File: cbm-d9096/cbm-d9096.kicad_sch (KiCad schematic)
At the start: 31 parts, among them J1 IEEE488 Header, J2 LED, J3 SD CARD, J4 WP/CD Jumper, J5 SD CARD, J6 WP/CD Jumper, J7 RESET, J8 Alt PWR, J9 Barrel_Jack, U1 ATmega1284-P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

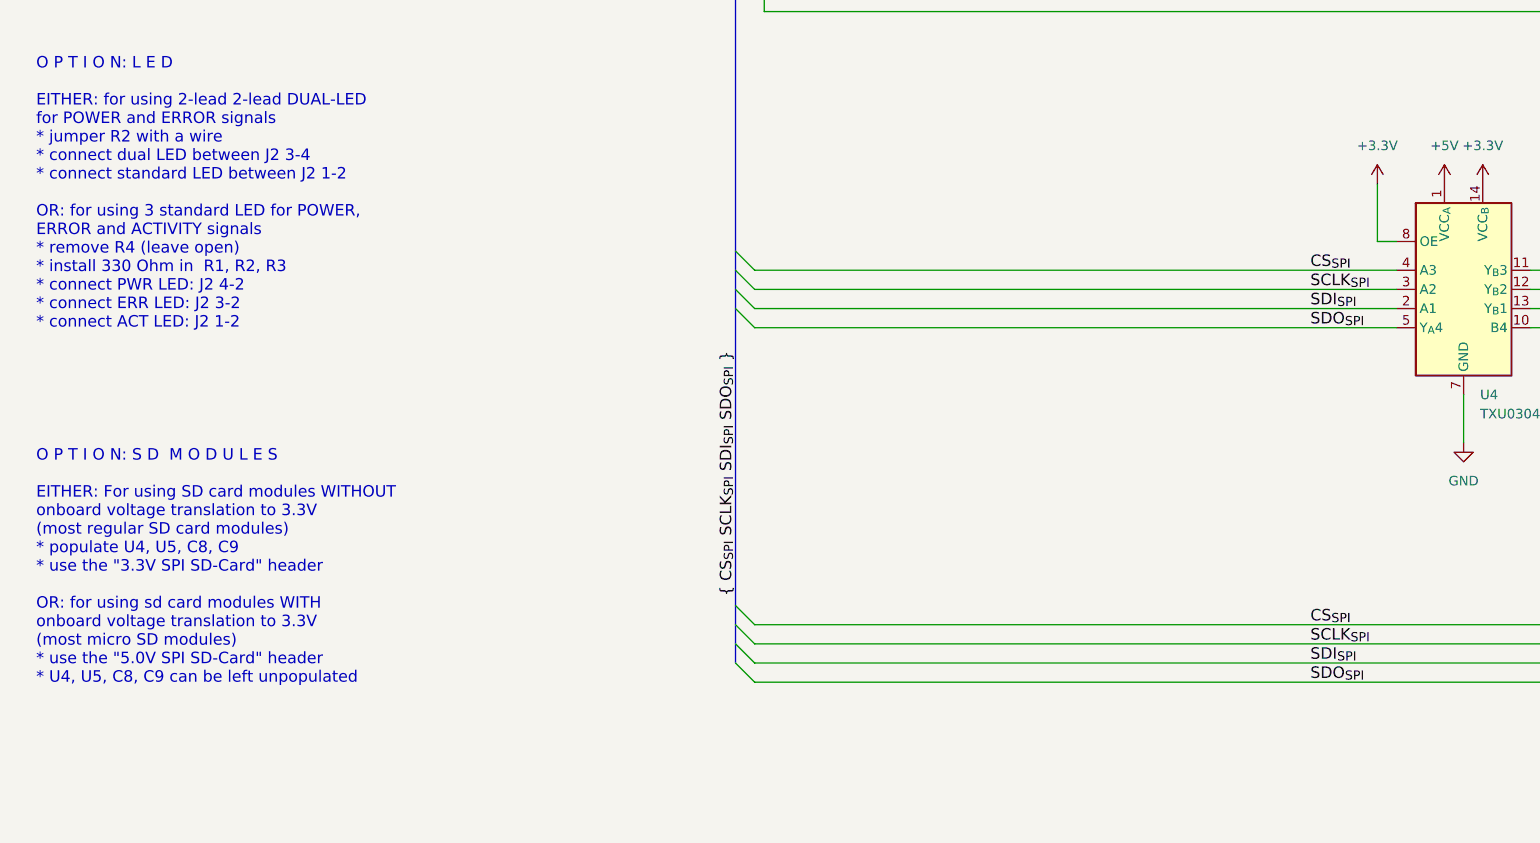
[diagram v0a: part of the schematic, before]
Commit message: added jumper to quickly enable/disable the level shifter
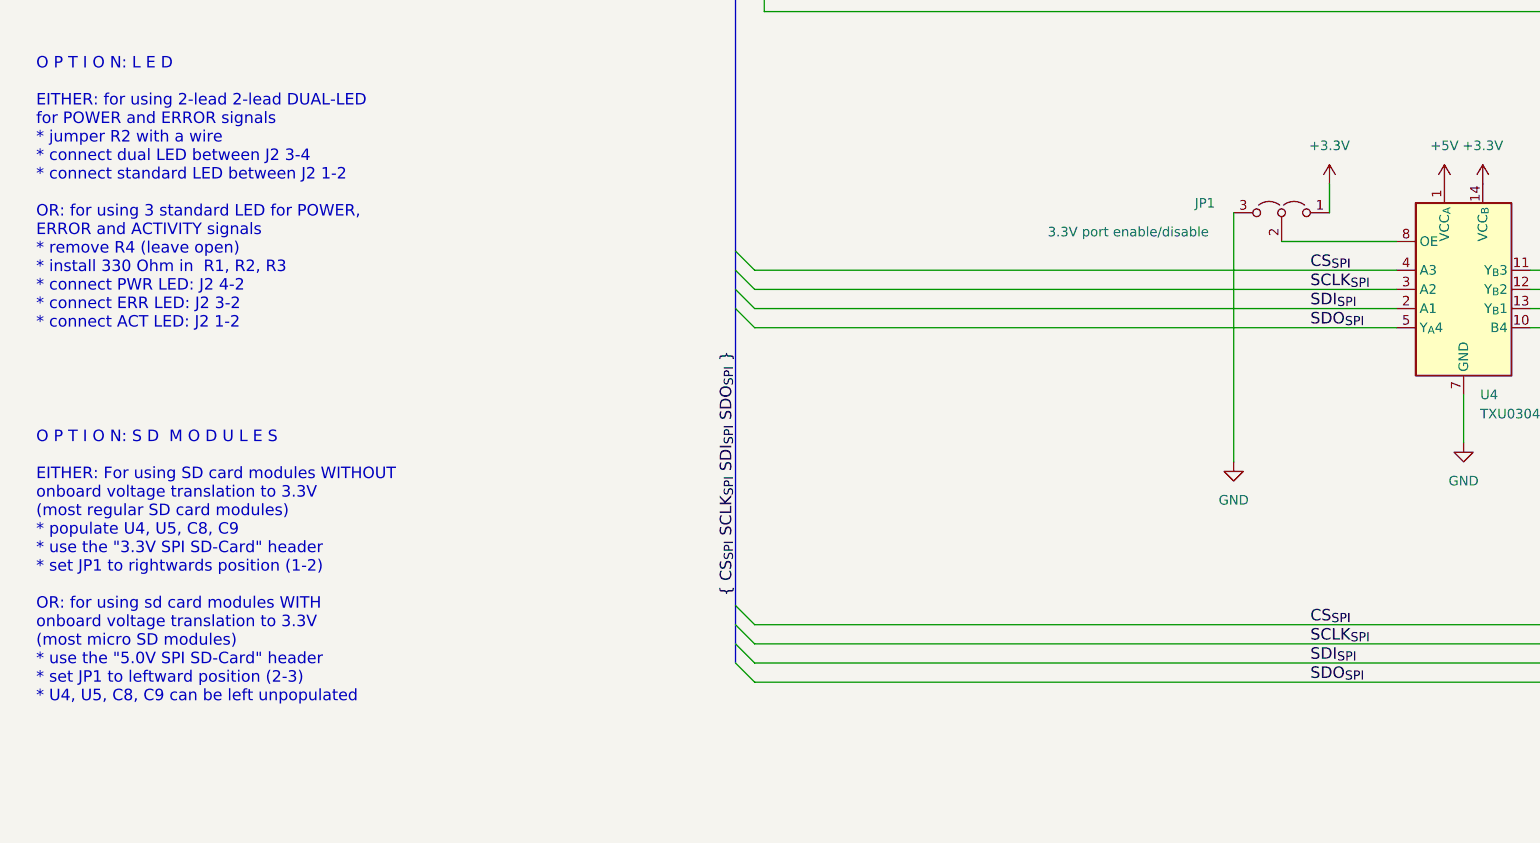
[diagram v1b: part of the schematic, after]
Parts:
- added JP1: 3.3V port enable/disable, Connector_PinHeader_2.00mm:PinHeader_1x03_P2.00mm_Vertical, symbol Jumper:Jumper_3_Open
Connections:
- net +3.3V: now also JP1.1 (A); no longer U4.8 (OE)
- net GND: now also JP1.3 (B)
- new net: JP1.2 (C), U4.8 (OE)
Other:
- note added: "O P T I O N: S D M O D U L E S EITHER: For using SD card modules WITHOUT onboard voltage translation to 3.3V (most regular SD card modules) * populate U4, U5, C8, C9 * use the "3.3V SPI SD-Card" header * set JP1 to rightwards position (1-2) OR: for using sd card modules WITH onboard voltage translation to 3.3V (most micro SD modules) * use the "5.0V SPI SD-Card" header * set JP1 to leftward posit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"
- note removed: "O P T I O N: S D M O D U L E S EITHER: For using SD card modules WITHOUT onboard voltage translation to 3.3V (most regular SD card modules) * populate U4, U5, C8, C9 * use the "3.3V SPI SD-Card" header OR: for using sd card modules WITH onboard voltage translation to 3.3V (most micro SD modules) * use the "5.0V SPI SD-Card" header * U4, U5, C8, C9 can be left unpopulated"
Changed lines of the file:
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@@
 	(title_block
 		(title "CBM D9096")
-		(date "2025-02-07")
-		(rev "1.1.0")
+		(date "2025-03-11")
+		(rev "1.1.1")
 		(comment 1 "based on work by Nils Eilers and Steve J. Gray")
 		(comment 2 "creativecommons.org/licenses/by-sa/4.0/")
@@
 		)
 	)
-	(text "O P T I O N: S D  M O D U L E S\n\nEITHER: For using SD card modules WITHOUT\nonboard voltage translation to 3.3V\n(most regular SD card modules)\n* populate U4, U5, C8, C9\n* use the \"3.3V SPI SD-Card\" header\n\nOR: for using sd card modules WITH\nonboard voltage translation to 3.3V\n(most micro SD modules)\n* use the \"5.0V SPI SD-Card\" header \n* U4, U5, C8, C9 can be left unpopulated"
+	(text "O P T I O N: S D  M O D U L E S\n\nEITHER: For using SD card modules WITHOUT\nonboard voltage translation to 3.3V\n(most regular SD card modules)\n* populate U4, U5, C8, C9\n* use the \"3.3V SPI SD-Card\" header\n* set JP1 to rightwards position (1-2)\n\nOR: for using sd card modules WITH\nonboard voltage translation to 3.3V\n(most micro SD modules)\n* use the \"5.0V SPI SD-Card\" header \n* set JP1 to leftward position (2-3)\n* U4, U5, C8, C9 can be left unpopulated"
 		(exclude_from_sim no)
 		(at 31.75 210.82 0)
@@
 	(wire
 		(pts
+			(xy 203.2 160.02) (xy 203.2 163.83)
+		)
+		(stroke
+			(width 0)
+			(type default)
+		)
+	)
+	(wire
+		(pts
 			(xy 313.69 236.22) (xy 322.58 236.22)
 		)
@@
 	(wire
 		(pts
+			(xy 190.5 163.83) (xy 190.5 196.85)
+		)
+		(stroke
+			(width 0)
+			(type default)
+		)
+	)
+	(wire
+		(pts
 			(xy 342.9 58.42) (xy 345.44 58.42)
 		)
@@
 	(wire
 		(pts
-			(xy 209.55 160.02) (xy 209.55 167.64)
-		)
-		(stroke
-			(width 0)
-			(type default)
-		)
-	)
-	(wire
-		(pts
 			(xy 342.9 53.34) (xy 345.44 53.34)
 		)
@@
 	(wire
 		(pts
+			(xy 196.85 167.64) (xy 212.09 167.64)
+		)
+		(stroke
+			(width 0)
+			(type default)
+		)
+	)
+	(wire
+		(pts
 			(xy 335.28 189.23) (xy 337.82 189.23)
 		)
@@
 	(wire
 		(pts
-			(xy 209.55 167.64) (xy 212.09 167.64)
-		)
-		(stroke
-			(width 0)
-			(type default)
-		)
-	)
-	(wire
-		(pts
 			(xy 128.27 273.05) (xy 115.57 273.05)
 		)
@@
 	)
 	(symbol
-		(lib_id "Device:C")
-		(at 38.1 43.18 90)
-		(mirror x)
+		(lib_id "power:+3.3V")
+		(at 203.2 160.02 0)
 		(unit 1)
 		(exclude_from_sim no)
@@
 		(dnp no)
 		(fields_autoplaced yes)
-		(property "Reference" "C6"
-			(at 38.1 35.56 90)
+		(property "Reference" "#PWR023"
+			(at 203.2 163.83 0)
 			(effects
 				(font
 					(size 1.27 1.27)
 				)
+				(hide yes)
 			)
 		)
-		(property "Value" "18 pF"
-			(at 38.1 38.1 90)
+		(property "Value" "+3.3V"
+			(at 203.2 154.94 0)
 			(effects
 				(font
@@
 			)
 		)
-		(property "Footprint" "Capacitor_THT:C_Disc_D3.8mm_W2.6mm_P2.50mm"
-			(at 41.91 44.1452 0)
+		(property "Footprint" ""
+			(at 203.2 160.02 0)
 			(effects
 				(font
@@
 			)
 		)
-		(property "Datasheet" "~"
-			(at 38.1 43.18 0)
+		(property "Datasheet" ""
+			(at 203.2 160.02 0)
 			(effects
 				(font
@@
 			)
 		)
-		(property "Description" "Unpolarized capacitor"
-			(at 38.1 43.18 0)
+		(property "Description" "Power symbol creates a global label with name \"+3.3V\""
+			(at 203.2 160.02 0)
 			(effects
 				(font
@@
 		(pin "1"
 		)
-		(pin "2"
-		)
 		(instances
 			(project "cbm-d9096"
 				(path "/0ff508fd-18da-4ab7-9844-3c8a28c2587e"
-					(reference "C6")
+					(reference "#PWR023")
 					(unit 1)
 				)
@@
 	)
 	(symbol
-		(lib_id "power:+5V")
-		(at 44.45 255.27 0)
+		(lib_id "Device:C")
+		(at 38.1 43.18 90)
+		(mirror x)
 		(unit 1)
 		(exclude_from_sim no)
@@
 		(dnp no)
 		(fields_autoplaced yes)
-		(property "Reference" "#PWR01"
-			(at 44.45 259.08 0)
+		(property "Reference" "C6"
+			(at 38.1 35.56 90)
 			(effects
 				(font
 					(size 1.27 1.27)
 				)
-				(hide yes)
 			)
 		)
-		(property "Value" "+5V"
-			(at 44.45 250.19 0)
+		(property "Value" "18 pF"
+			(at 38.1 38.1 90)
 			(effects
 				(font
@@
 			)
 		)
-		(property "Footprint" ""
-			(at 44.45 255.27 0)
+		(property "Footprint" "Capacitor_THT:C_Disc_D3.8mm_W2.6mm_P2.50mm"
+			(at 41.91 44.1452 0)
 			(effects
 				(font
@@
 			)
 		)
-		(property "Datasheet" ""
-			(at 44.45 255.27 0)
+		(property "Datasheet" "~"
+			(at 38.1 43.18 0)
 			(effects
 				(font
@@
 			)
 		)
-		(property "Description" "Power symbol creates a global label with name \"+5V\""
-			(at 44.45 255.27 0)
+		(property "Description" "Unpolarized capacitor"
+			(at 38.1 43.18 0)
 			(effects
 				(font
@@
 		(pin "1"
 		)
+		(pin "2"
+		)
 		(instances
 			(project "cbm-d9096"
 				(path "/0ff508fd-18da-4ab7-9844-3c8a28c2587e"
-					(reference "#PWR01")
+					(reference "C6")
 					(unit 1)
 				)
@@
 	)
 	(symbol
-		(lib_id "power:+3.3V")
-		(at 223.52 160.02 0)
+		(lib_id "power:+5V")
+		(at 44.45 255.27 0)
 		(unit 1)
 		(exclude_from_sim no)
@@
 		(dnp no)
 		(fields_autoplaced yes)
-		(property "Reference" "#PWR019"
-			(at 223.52 163.83 0)
+		(property "Reference" "#PWR01"
+			(at 44.45 259.08 0)
 			(effects
 				(font
@@
 			)
 		)
-		(property "Value" "+3.3V"
-			(at 223.52 154.94 0)
+		(property "Value" "+5V"
+			(at 44.45 250.19 0)
 			(effects
 				(font
@@
 		)
 		(property "Footprint" ""
-			(at 223.52 160.02 0)
+			(at 44.45 255.27 0)
 			(effects
 				(font
@@
 		)
 		(property "Datasheet" ""
-			(at 223.52 160.02 0)
+			(at 44.45 255.27 0)
 			(effects
 				(font
@@
 			)
 		)
-		(property "Description" "Power symbol creates a global label with name \"+3.3V\""
-			(at 223.52 160.02 0)
+		(property "Description" "Power symbol creates a global label with name \"+5V\""
+			(at 44.45 255.27 0)
 			(effects
 				(font
@@
 		)
 		(instances
-			(project ""
+			(project "cbm-d9096"
 				(path "/0ff508fd-18da-4ab7-9844-3c8a28c2587e"
-					(reference "#PWR019")
+					(reference "#PWR01")
 					(unit 1)
 				)
@@
 	(symbol
 		(lib_id "power:+3.3V")
-		(at 209.55 160.02 0)
+		(at 223.52 160.02 0)
 		(unit 1)
 		(exclude_from_sim no)
@@
 		(dnp no)
 		(fields_autoplaced yes)
-		(property "Reference" "#PWR012"
-			(at 209.55 163.83 0)
+		(property "Reference" "#PWR019"
+			(at 223.52 163.83 0)
 			(effects
 				(font
@@
 		)
 		(property "Value" "+3.3V"
-			(at 209.55 154.94 0)
+			(at 223.52 154.94 0)
 			(effects
 				(font
@@
 		)
 		(property "Footprint" ""
-			(at 209.55 160.02 0)
+			(at 223.52 160.02 0)
 			(effects
 				(font
@@
 		)
 		(property "Datasheet" ""
-			(at 209.55 160.02 0)
+			(at 223.52 160.02 0)
 			(effects
 				(font
@@
 		)
 		(property "Description" "Power symbol creates a global label with name \"+3.3V\""
-			(at 209.55 160.02 0)
+			(at 223.52 160.02 0)
 			(effects
 				(font
@@
 		)
 		(instances
-			(project "cbm-d9096"
+			(project ""
 				(path "/0ff508fd-18da-4ab7-9844-3c8a28c2587e"
-					(reference "#PWR012")
+					(reference "#PWR019")
 					(unit 1)
 				)
@@
 	)
 	(symbol
+		(lib_id "power:GND")
+		(at 190.5 196.85 0)
+		(unit 1)
+		(exclude_from_sim no)
+		(in_bom yes)
+		(on_board yes)
+		(dnp no)
+		(fields_autoplaced yes)
+		(property "Reference" "#PWR012"
+			(at 190.5 203.2 0)
+			(effects
+				(font
+					(size 1.27 1.27)
+				)
+				(hide yes)
+			)
+		)
+		(property "Value" "GND"
+			(at 190.5 201.93 0)
+			(effects
+				(font
+					(size 1.27 1.27)
+				)
+			)
+		)
+		(property "Footprint" ""
+			(at 190.5 196.85 0)
+			(effects
+				(font
+					(size 1.27 1.27)
+				)
+				(hide yes)
+			)
+		)
+		(property "Datasheet" ""
+			(at 190.5 196.85 0)
+			(effects
+				(font
+					(size 1.27 1.27)
+				)
+				(hide yes)
+			)
+		)
+		(property "Description" "Power symbol creates a global label with name \"GND\" , ground"
+			(at 190.5 196.85 0)
+			(effects
+				(font
+					(size 1.27 1.27)
+				)
+				(hide yes)
+			)
+		)
+		(pin "1"
+		)
+		(instances
+			(project "cbm-d9096"
+				(path "/0ff508fd-18da-4ab7-9844-3c8a28c2587e"
+					(reference "#PWR012")
+					(unit 1)
+				)
+			)
+		)
+	)
+	(symbol
 		(lib_id "Device:R_Network05_Split")
 		(at 209.55 85.09 0)
@@
 					(unit 1)
 				)
+			)
+		)
+	)
+	(symbol
+		(lib_id "Jumper:Jumper_3_Open")
+		(at 196.85 163.83 0)
+		(mirror y)
+		(unit 1)
+		(exclude_from_sim yes)
+		(in_bom yes)
+		(on_board yes)
+		(dnp no)
+		(property "Reference" "JP1"
+			(at 186.69 162.56 0)
+			(effects
+				(font
+					(size 1.27 1.27)
+				)
+			)
+		)
+		(property "Value" "3.3V port enable/disable"
+			(at 176.53 166.37 0)
+			(effects
+				(font
+					(size 1.27 1.27)
+				)
+			)
+		)
+		(property "Footprint" "Connector_PinHeader_2.00mm:PinHeader_1x03_P2.00mm_Vertical"
+			(at 196.85 163.83 0)
+			(effects
+				(font
+					(size 1.27 1.27)
+				)
+				(hide yes)
+			)
+		)
+		(property "Datasheet" "~"
+			(at 196.85 163.83 0)
+			(effects
+				(font
+					(size 1.27 1.27)
+				)
+				(hide yes)
+			)
+		)
+		(property "Description" "Jumper, 3-pole, both open"
+			(at 196.85 163.83 0)
+			(effects
+				(font
+					(size 1.27 1.27)
+				)
+				(hide yes)
+			)
+		)
+		(pin "3"
+		)
+		(pin "2"
+		)
+		(pin "1"
+		)
+		(instances
+			(project ""
+				(path "/0ff508fd-18da-4ab7-9844-3c8a28c2587e"
+					(reference "JP1")
+					(unit 1)
+				)
